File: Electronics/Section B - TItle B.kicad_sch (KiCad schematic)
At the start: 32 parts, among them J10 JST_SHBM04B-SRSS-TB, J11 JST_SHBM04B-SRSS-TB, J12 JST_SHBM04B-SRSS-TB, J13 JST_SHBM04B-SRSS-TB, J14 JST_SHBM04B-SRSS-TB, J4 THD-20-R, J5 RJ45_RB1-125B8G1A, J6 Conn_01x07, J7 Micro_SD_Card_Det, J8 Conn_01x04, J9 Conn_02x07_Odd_Even, Q1 PMOS, SW1 Right angle Tact button, U2 TPD4EUSB30, U3 TPD4EUSB30, U4 74LVC1G07SE-7, U5 RT9742GGJ5

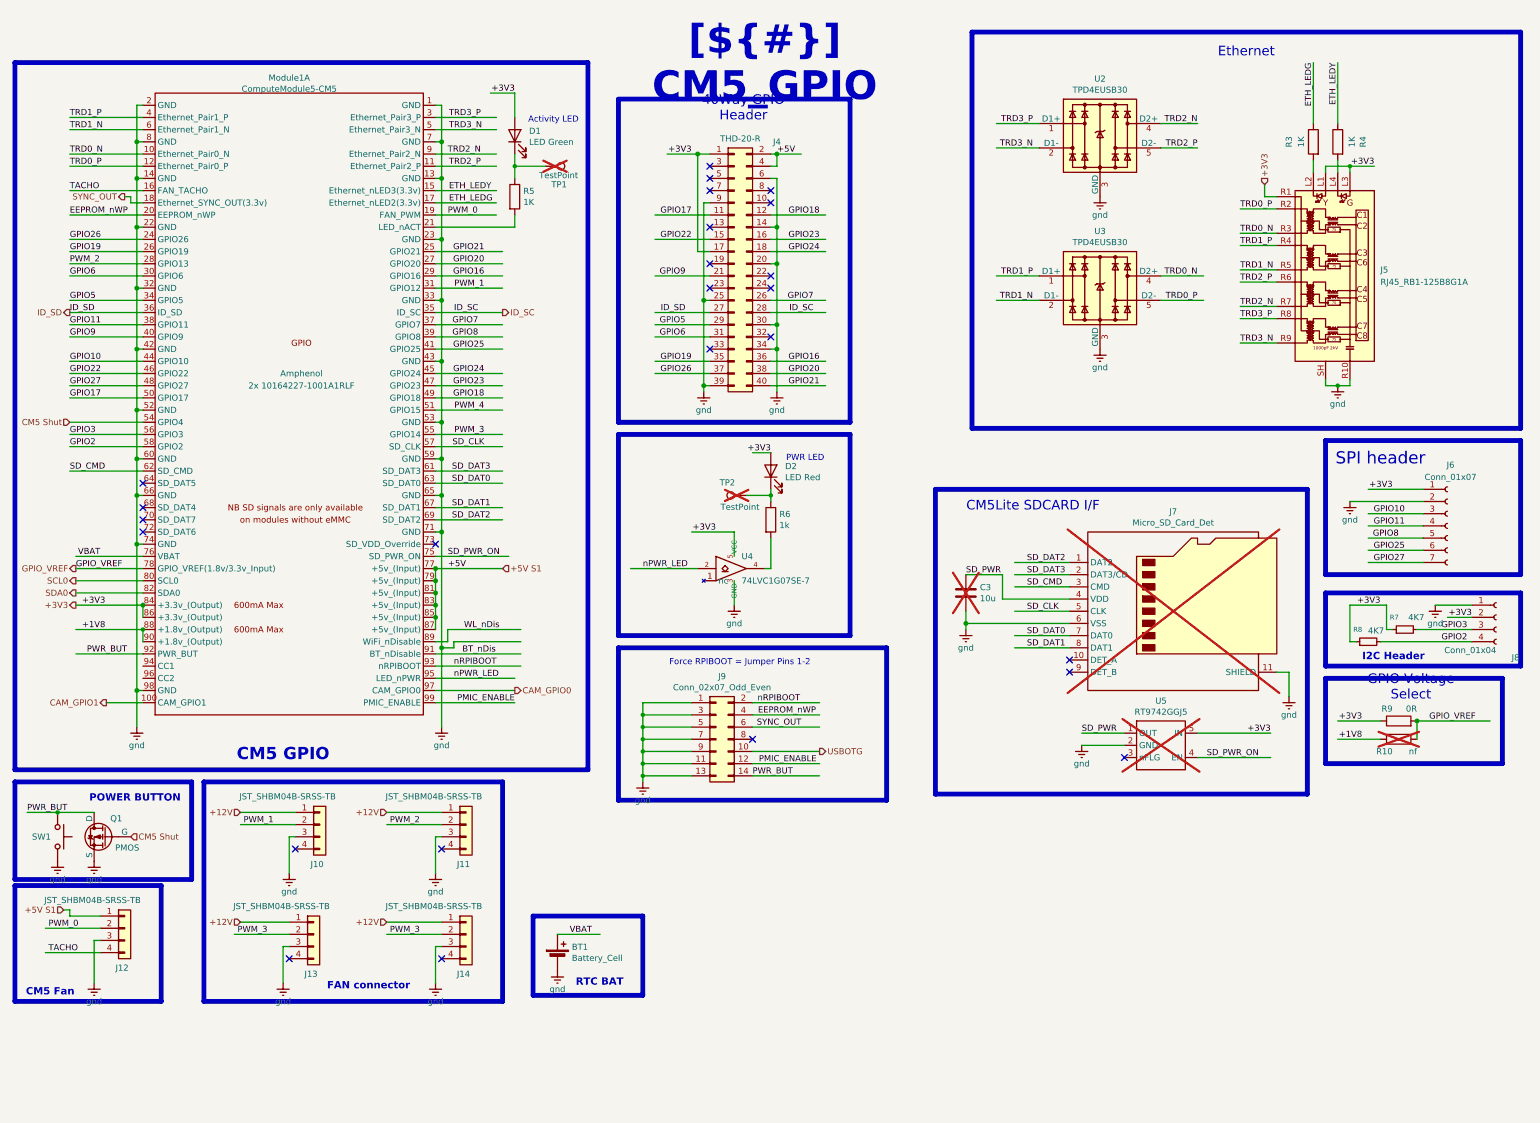
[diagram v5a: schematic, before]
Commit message: Sata Port Changed
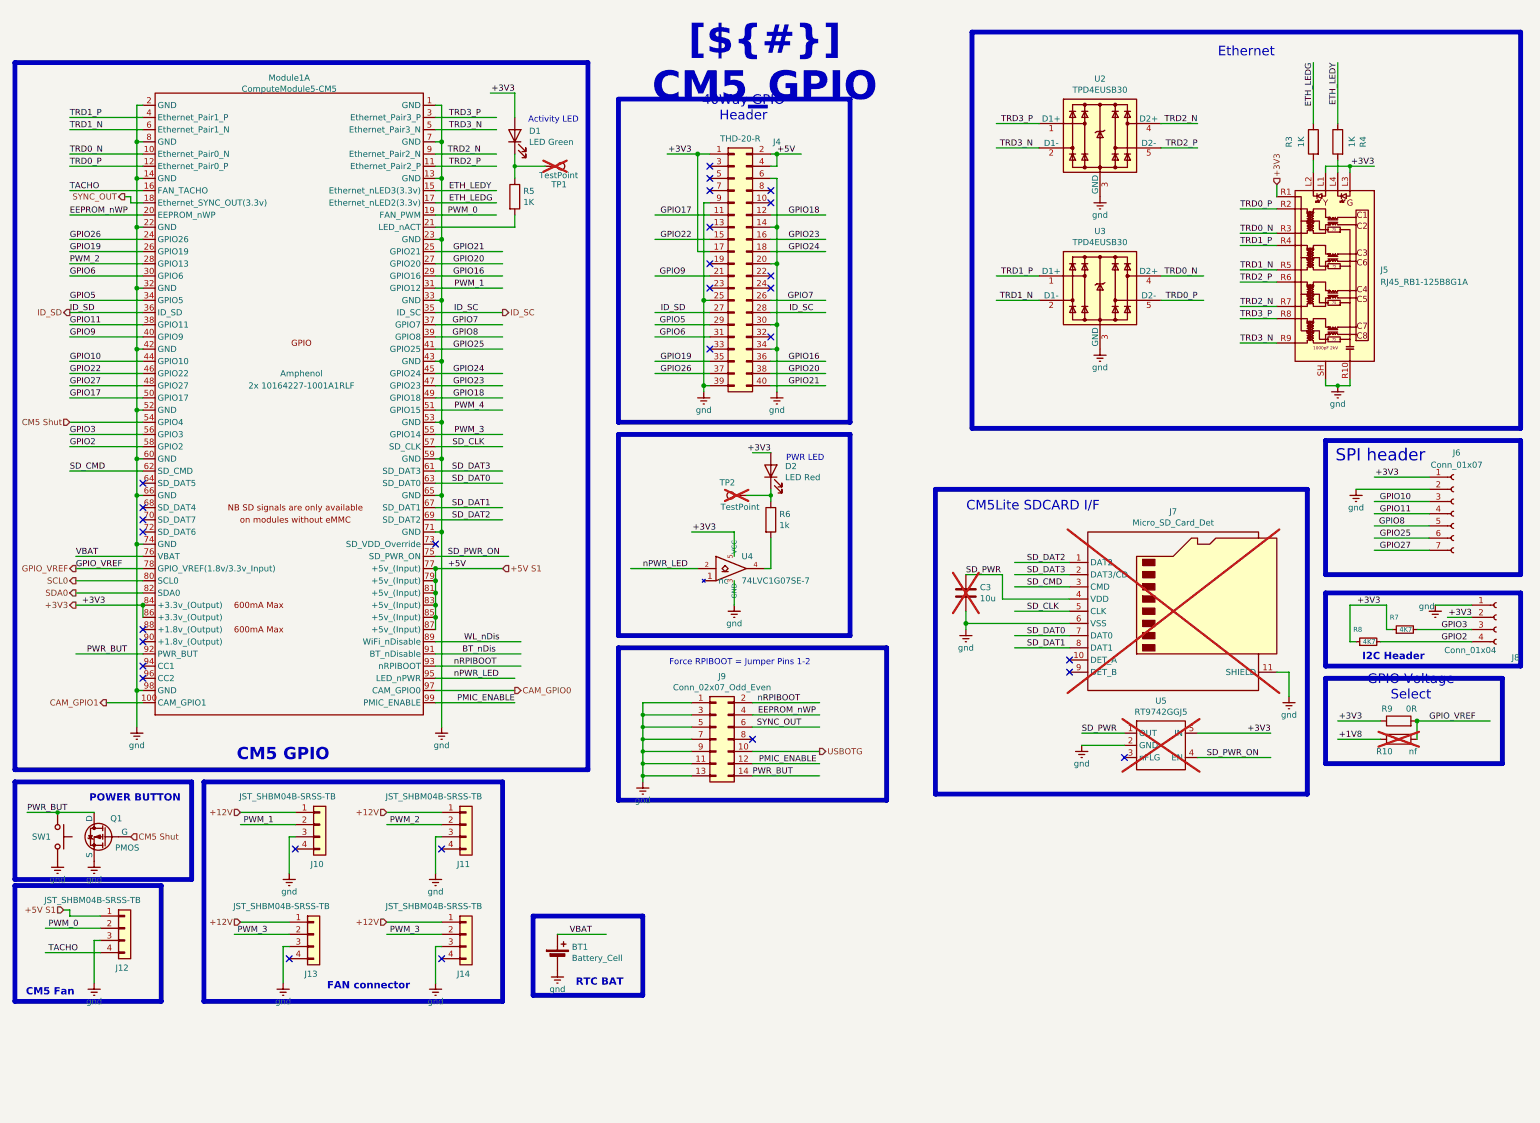
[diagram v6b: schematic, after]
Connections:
- net +1V8: no longer Module1.88 (+1.8v_(Output)), Module1.90 (+1.8v_(Output))
- no-connect marks 25 -> 29
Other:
- moved on the sheet: J6

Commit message: Changed sata port
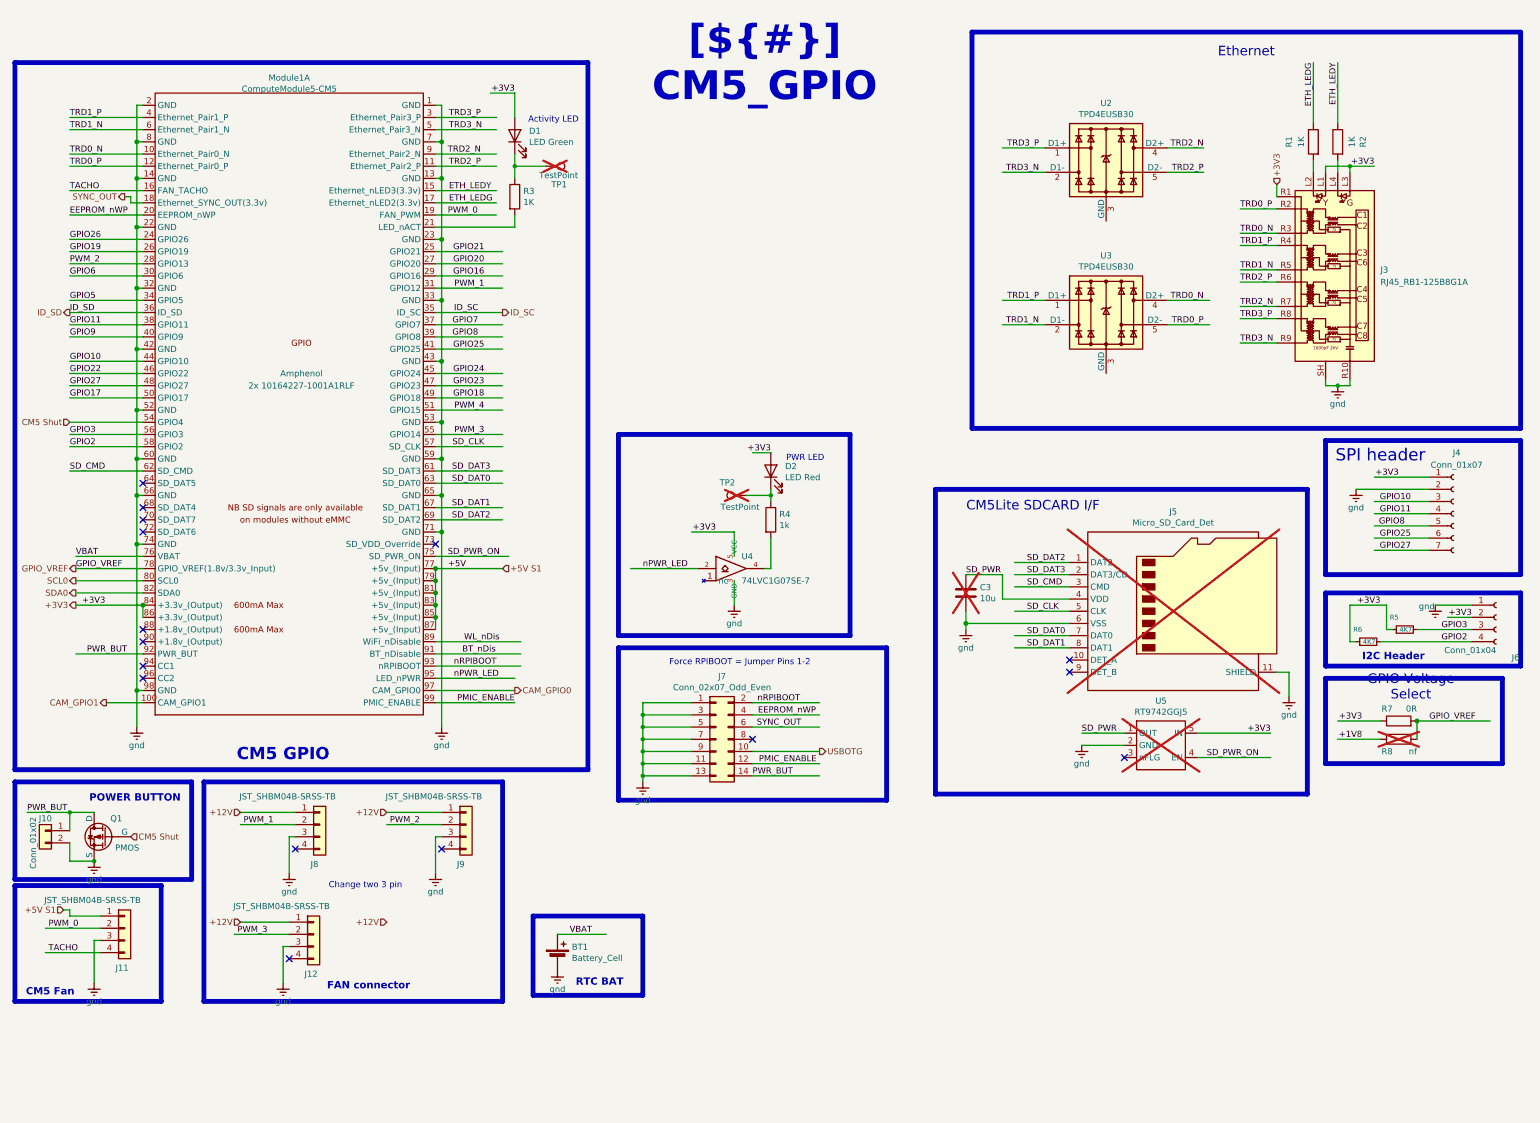
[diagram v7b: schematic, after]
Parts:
- removed J14: JST_SHBM04B-SRSS-TB, Connector_JST:JST_SH_BM04B-SRSS-TB_1x04-1MP_P1.00mm_Vertical, symbol Connector_Generic:Conn_01x04
- removed J4: THD-20-R, Connector_PinHeader_2.54mm:PinHeader_2x20_P2.54mm_Vertical, symbol Connector_Generic:Conn_02x20_Odd_Even
- removed SW1: Right angle Tact button, Button_Switch_THT:SW_Tactile_SPST_Angled_PTS645Vx58-2LFS, symbol Switch:SW_Push
- added J10: Conn_01x02, Connector_JST:JST_GH_BM02B-GHS-TBT_1x02-1MP_P1.25mm_Vertical, symbol Connector_Generic:Conn_01x02
- renumbered J12 to J11, J13 to J12, J5 to J3, J6 to J4, J7 to J5, J8 to J6, J9 to J7, J10 to J8, J11 to J9, R3 to R1, R4 to R2, R5 to R3, R6 to R4, R7 to R5, R8 to R6, R9 to R7, R10 to R8
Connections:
- net PWR_BUT: now also J10.1 (Pin_1)
- net gnd: now also J10.2 (Pin_2); no longer U2.3 (GND), U2.8 (GND), U3.3 (GND), U3.8 (GND)
- new net: U3.3 (GND), U3.8 (GND)
- new net: U2.3 (GND), U2.8 (GND)
- no-connect marks 29 -> 16
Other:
- note added: "Change two 3 pin"
